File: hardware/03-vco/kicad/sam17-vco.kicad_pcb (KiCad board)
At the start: 4 copper layers, 114 x 124 mm, 140 parts, among them J1 Molex_KK-254_AE-6410-04A_1x04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, J2 IDC-Header_2x06_P2.54mm_Verti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, U1 QFN-32-1EP_4x4mm_P0.4mm_EP2.6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, U10 SOIC-14_3.9x8.7mm_P1.27mm, U11 SOT-89-3, U12 SOT-223-3_TabPin2, U13 VSSOP-8_3x3mm_P0.65mm, U14 SOT-23-5, U2 QFN-32-1EP_4x4mm_P0.4mm_EP2.6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, U3 QFN-32-1EP_4x4mm_P0.4mm_EP2.6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, U4 QFN-32-1EP_4x4mm_P0.4mm_EP2.6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, U5 TSSOP-16_4.4x5mm_P0.65mm, U6 TSSOP-16_4.4x5mm_P0.65mm, U7 TSSOP-16_4.4x5mm_P0.65mm, U8 SOIC-8_3.9x4.9mm_P1.27mm, U9 SOIC-14_3.9x8.7mm_P1.27mm

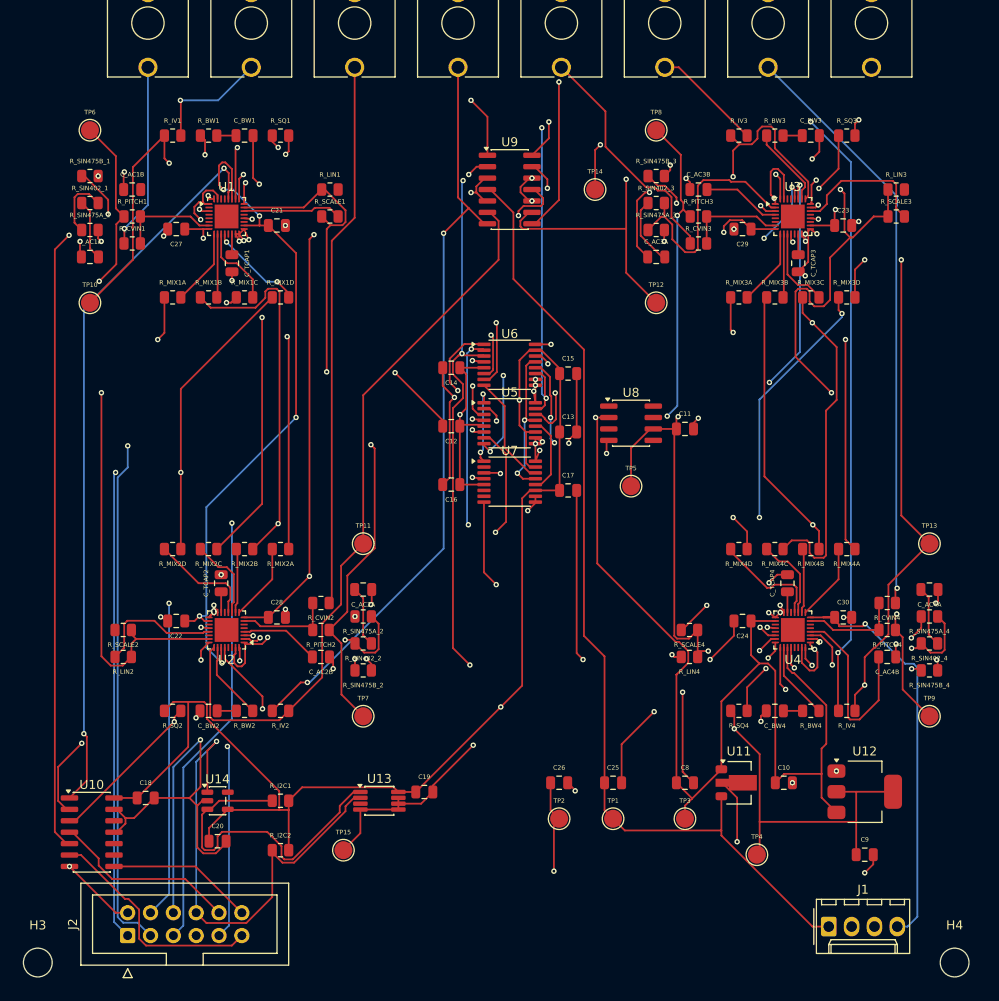
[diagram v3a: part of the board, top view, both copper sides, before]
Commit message: Modulo 3 VCO: los escapes explicitos se miden y se descartan (Tarea 6, ronda 5)
El controlador autorizo escribir escapes explicitos (pin -> via, cortos,
antes del ruteo, protegidos en el DSN) para el abanico del costado derecho
de los QFN, con la misma filosofia que las siete costuras de masa. Lo
implemente tal cual y lo medi en dos variantes. Sale peor, consistente:

  sin escapes de senal (cinco corridas):        4, 5, 8, 9, 10 abiertas
  + 20 escapes (pines 2,3,4,21,22), protegidos: 16
  + 8 escapes (solo 21 y 22), protegidos ronda 1: 12
  revertido a solo costuras de masa (comiteado): 11

Las dos variantes de escape quedan por debajo del PEOR sorteo del baseline,
asi que no es mala suerte.

La diferencia con las costuras de masa, que si funcionaron, es si el pin
tiene alternativa. El pin 20 del QFN y el 4 del TSSOP tienen un pasillo de
1 a 1.45 mm que da para una via y nada mas: reservarla es ganancia neta
porque le quitamos al router un sitio que no le servia para otra cosa. Los
pines 21 y 22 SI tienen alternativas -- arriba, abajo, en diagonal,
compartiendo carril -- y al reservarles una via les fijamos una sola salida
y ademas le quitamos a los otros veintisiete pines del mismo anillo el hueco
que necesitaban para su propio fanout. En el anillo de un QFN de 0.4 mm de
paso el cobre es un juego de suma cero, y el router reparte mejor que yo.

La leccion, que queda escrita en el script junto a los numeros: pre-colocar
funciona donde la geometria fuerza una unica solucion y estorba donde hay
varias.

DONDE QUEDA: DRC 0, In1 sin pistas y al 99.97% en una isla, costuras de masa
cerradas (0 pads sin bajada), frontera 3.00 mm, los 4 EP aislados, DAC->VCO
43.2 mm, desacoplos a 1.80 mm. Quedan 11 conexiones abiertas, diez de ellas
pines de QFN que no atraviesan su propio anillo de escape (1, 2, 21, 22, 23,
25, 26, 31: siempre los que van detras en la cola de su costado). Van en el
reporte con coordenada y motivo. El numero depende de la semilla del router
y no del dise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
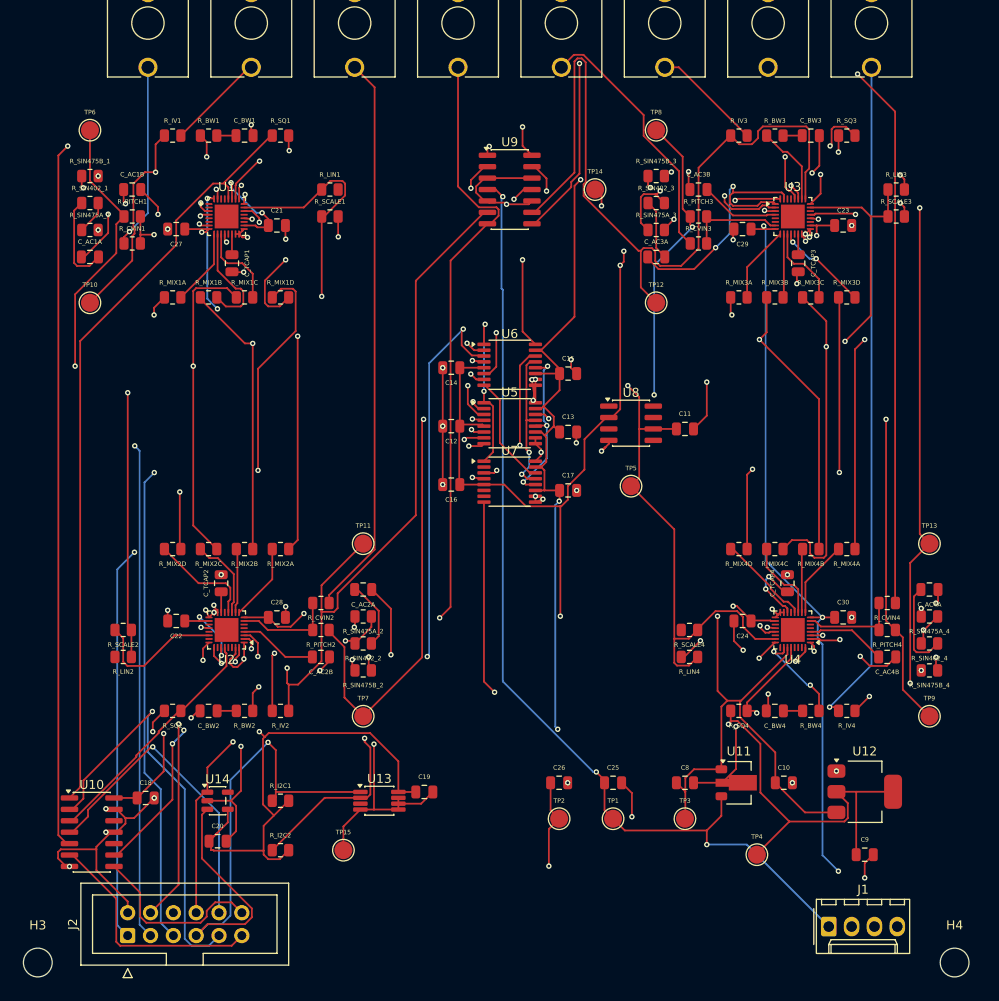
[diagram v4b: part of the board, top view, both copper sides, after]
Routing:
- net SQ_4: track 11.2 -> 92.1 mm, vias 2 -> 3
- net GNDA: track 170.1 -> 125.0 mm, vias 82 -> 76
- net VREF_2V5: track 292.8 -> 259.0 mm, vias 11 -> 6
- net GNDD: track 112.6 -> 79.9 mm, vias 4 -> 8
- net MIX_SAW: track 152.0 -> 120.8 mm, vias 4 -> 3
- net MIXO_3: track 61.6 -> 92.1 mm, vias 2 -> 0
- net I2C_SDA: track 36.8 -> 63.8 mm, vias 0 -> 1
- net MIX_TRI: track 116.0 -> 140.0 mm
- net N21_3: track 0.00 -> 19.9 mm, vias 0 -> 2
- net +5V_LOC: track 308.7 -> 293.2 mm, vias 10 -> 11
- net N22_2: track 0.00 -> 15.1 mm
- net TUNE_OUT_2: track 20.8 -> 35.1 mm, vias 0 -> 1
- net N21_2: track 14.3 -> 0.00 mm
- net N22_3: track 15.6 -> 1.69 mm, vias 0 -> 1
- net N22_4: track 13.0 -> 0.00 mm, vias 2 -> 0
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
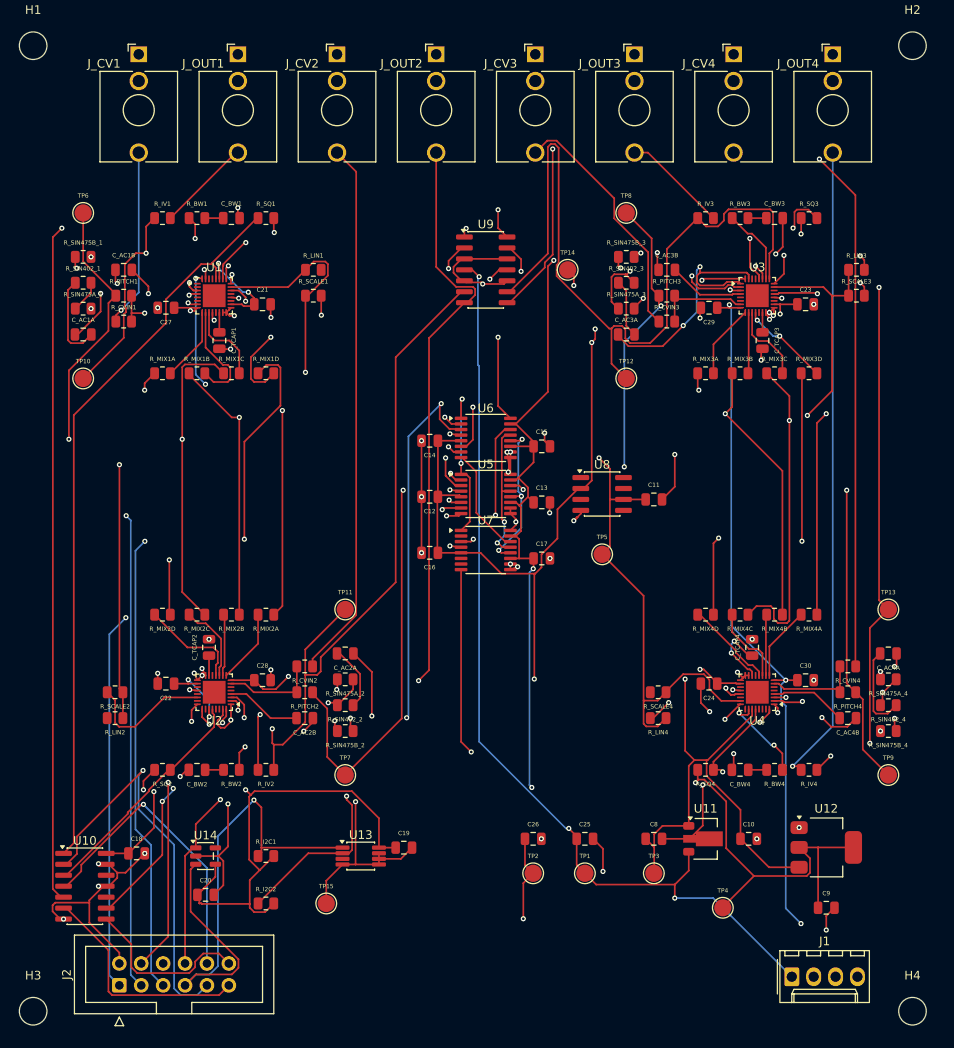
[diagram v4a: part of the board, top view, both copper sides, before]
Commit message: Modulo 3 VCO: reglas a la capacidad real del fab, y la placa CIERRA (Tarea 6)
0 conexiones abiertas y DRC 0. Con todos los demas gates en verde: In1 en
UNA sola isla al 100.00%, costuras de masa cerradas, frontera 3.00 mm, los
4 EP aislados, DAC->VCO 43.2 mm, desacoplos a 1.80 mm. El recorrido de la
tarea fue 165 -> 18 (2 capas) -> 8 -> 11 -> 0.

Las dos "paredes aritmeticas" que declare en la ronda 6 eran de MIS reglas,
no del fabricante. Via 0.6, margen 0.15 y pista 0.2 venian heredadas del
modulo 2 -- una placa de dos capas con componentes de paso ancho -- y nunca
les volvi a preguntar nada. Calcule bien y verifique mal: la formula
VIA_D/2 + CLEARANCE + ANCHO/2 = 0.55 > 0.40 era correcta, pero no mire la
hoja de capacidades del fabricante ni una sola vez antes de escribir
"taladro laser, proceso HDI, otra liga".

Verificado en jlcpcb.com/capabilities/pcb-capabilities el 2026-08-17,
proceso ESTANDAR de 4 capas en 1 oz, sin HDI y sin via-in-pad: pista y
aislamiento minimos 0.09/0.09 mm, taladro de via minimo 0.15, y sin recargo
un taladro de 0.20 si el diametro es >= 0.45 ("0.2mm or 0.25mm hole size
with via diameter less than 0.45mm, will cost more" -- por eso 0.45 y no el
0.40 sugerido: 0.45/0.20 es justo el punto sin recargo). Las reglas quedan
en pista 0.12, aislamiento 0.10, via 0.45/0.20: un 30% por encima del minimo
publicado. La aritmetica del escape pasa de 0.550 a 0.385 contra los 0.400
de paso del QFN, y queda como comprobacion ejecutable en _check_escape().

Con eso el ruteo cerro entero, pero aparecieron 108 infracciones de
hole_clearance: otro default de KiCad (0.25 mm) que tampoco habia elegido
nadie. El fabricante pide 0.20 de taladro de via a pista y el ruteo consigue
0.235 (anillo 0.125 + margen 0.11). Puesto el valor verificado, 0
infracciones -- no es relajar el checker, es que examinaba de una regla
inventada. KiCad tiene un solo campo de margen de taladro y el fabricante
pide 0.28 para PTH, asi que ese caso lo comprobe aparte sobre los 44
tala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
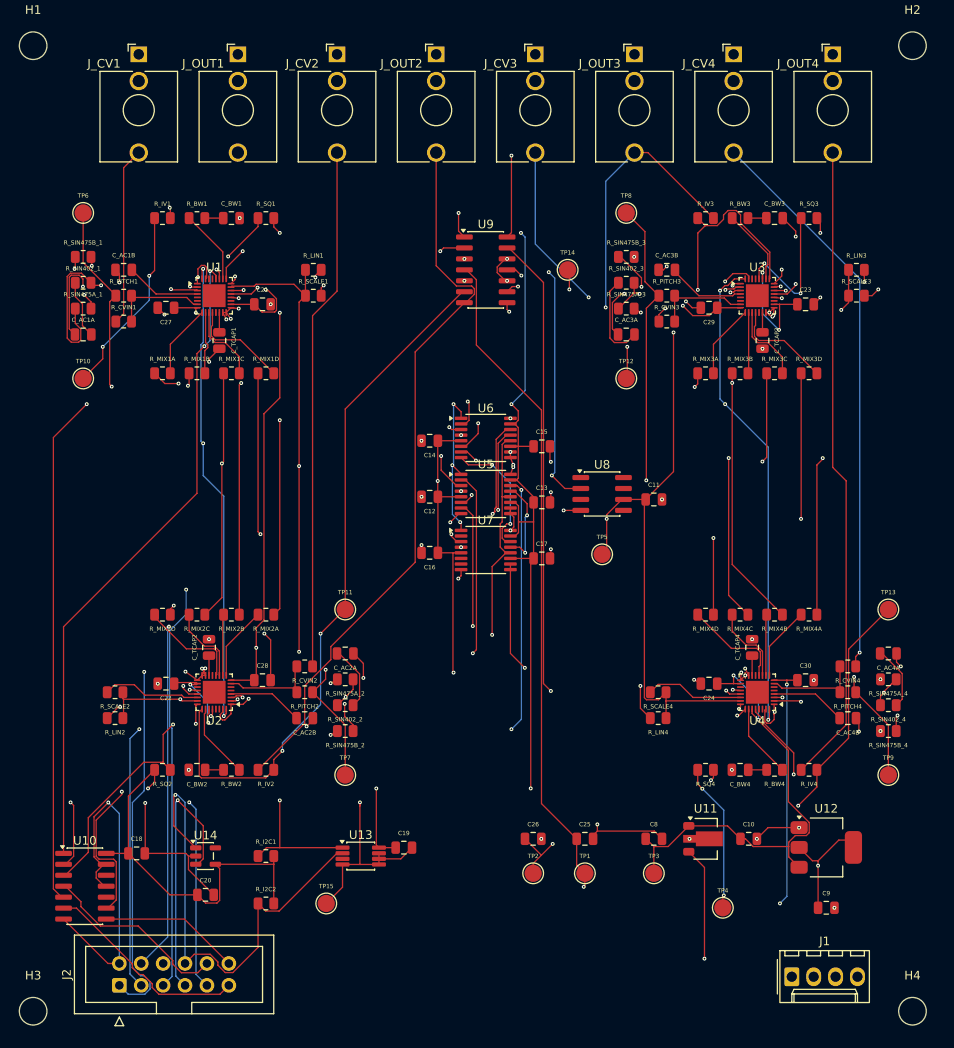
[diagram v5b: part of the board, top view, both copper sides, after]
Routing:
- net GNDA: track 125.0 -> 85.9 mm, vias 76 -> 82
- net MIXO_3: track 92.1 -> 55.9 mm, vias 0 -> 3
- net GNDD: track 79.9 -> 110.3 mm, vias 8 -> 4
- net N2_1: track 3.76 -> 28.9 mm, vias 0 -> 2
- net VREF_2V5: track 259.0 -> 234.9 mm, vias 6 -> 10
- net MIX_PULSE: track 145.5 -> 123.7 mm, vias 3 -> 4
- net PWM_CV: track 193.6 -> 176.2 mm
- net SQ_4: track 92.1 -> 106.8 mm
- net N22_3: track 1.69 -> 16.4 mm, vias 1 -> 2
- net +3V3_LOC: track 323.6 -> 309.5 mm, vias 9 -> 10
- net N21_2: track 0.00 -> 13.8 mm, vias 0 -> 2
- net TUNE_OUT_2: track 35.1 -> 21.8 mm, vias 1 -> 0
- net -12V: track 273.2 -> 260.4 mm, vias 7 -> 8
- net N21_1: track 0.00 -> 11.7 mm, vias 0 -> 2
- net CV_PITCH_4: track 85.7 -> 74.2 mm
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
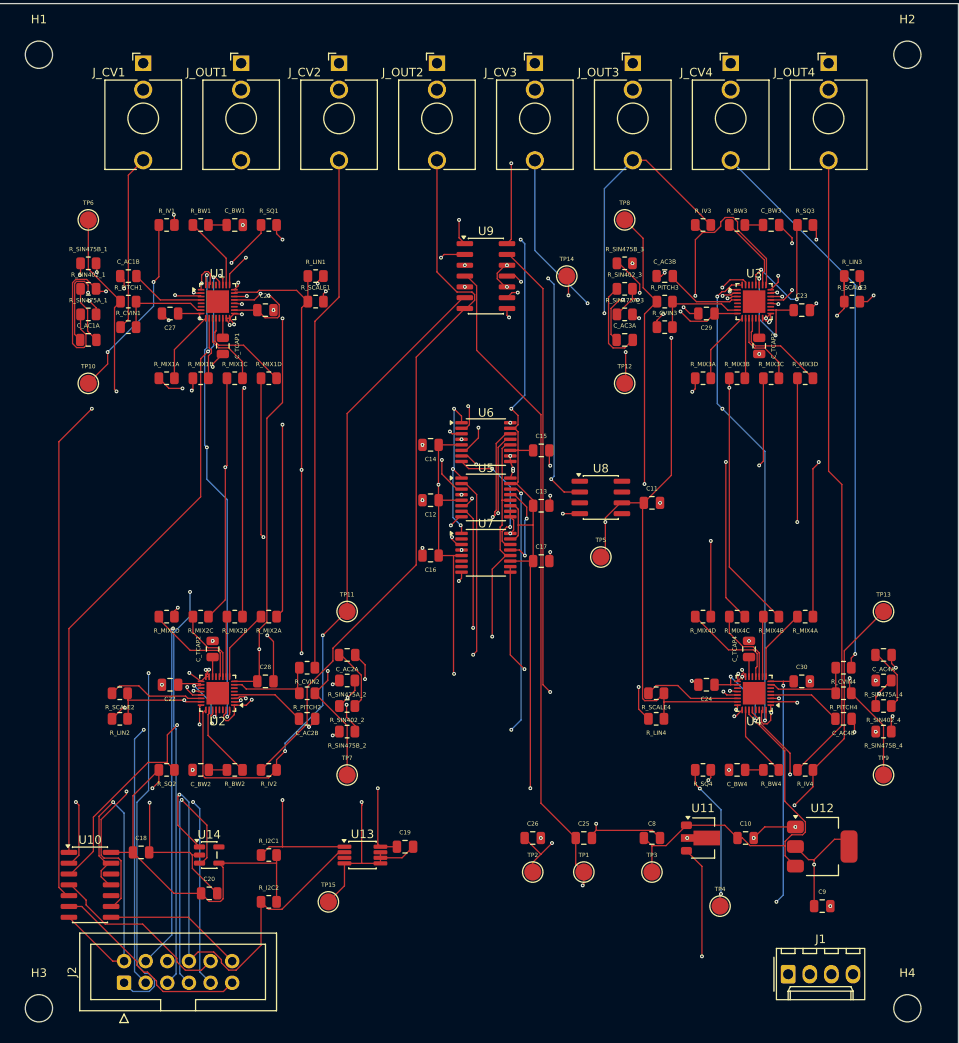
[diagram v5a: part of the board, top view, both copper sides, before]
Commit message: Modulo 3 VCO: vias fuera de los pads, serigrafia legible y U13 con los osciladores
La placa de la tanda anterior pasaba el gate porque el gate no miraba. Con
hole_to_hole y holes_co_located en la severidad que les corresponde, aquella
placa tiene 33 infracciones: 15 vias taladradas DENTRO del agujero de un jack
o de un conector (solapes de -0.81 mm, la broca pasando dos veces por el mismo
punto), 32 vias debajo de un pad SMD, y 3 parejas de vias por debajo del
minimo de taladro a taladro, una a 0.0000 mm.

El origen eran tres cosas y solo dos estaban a la vista. coser_masas() probaba
el CENTRO DEL PAD como primer sitio para la via. lejos() se salta el cobre de
la propia red -- correcto para un corto, equivocado para una broca, que no lee
el netlist. Y la tercera, que producia las ocho peores: en el manguito de un
jack el pad ESTA en el centro de la huella, asi que el rumbo del abanico salia
(0,0) y sus 110 candidatos degeneraban en un unico punto, el propio centro del
pad; con el yield del centro delante nadie lo noto en siete rondas.

Ahora el margen electrico y el mecanico son dos funciones con dos significados
-- lejos() y taladro_libre() --, la via va AL LADO del pad con su rabito (el
pasillo de 1 a 1.45 mm de la ronda 4 da para eso con via de 0.45), las dos
reglas de taladro son ERROR en el .kicad_pro, y revisar_taladros() lo vuelve a
medir sobre la placa terminada preguntandole a la FORMA real del pad y no a su
caja. Esa comprobacion se gano el sueldo: su primer falso positivo obligo a
medir bien, y al medir bien aparecio un defecto que nadie tenia visto, cuatro
vias de masa taladradas sobre la corona de los jacks.

La serigrafia iba a 0.5 mm de alto citando el minimo de PISTA del fabricante.
La misma hoja pide 1.0 mm de alto y 0.15 de trazo para el texto, y son dos
especificaciones distintas. Eran 112 avisos de text_height y una placa que
violaba su propio minimo declarado. Se arregla como lo hace la industria en
SMD: se ocultan las referencias de los pasivos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
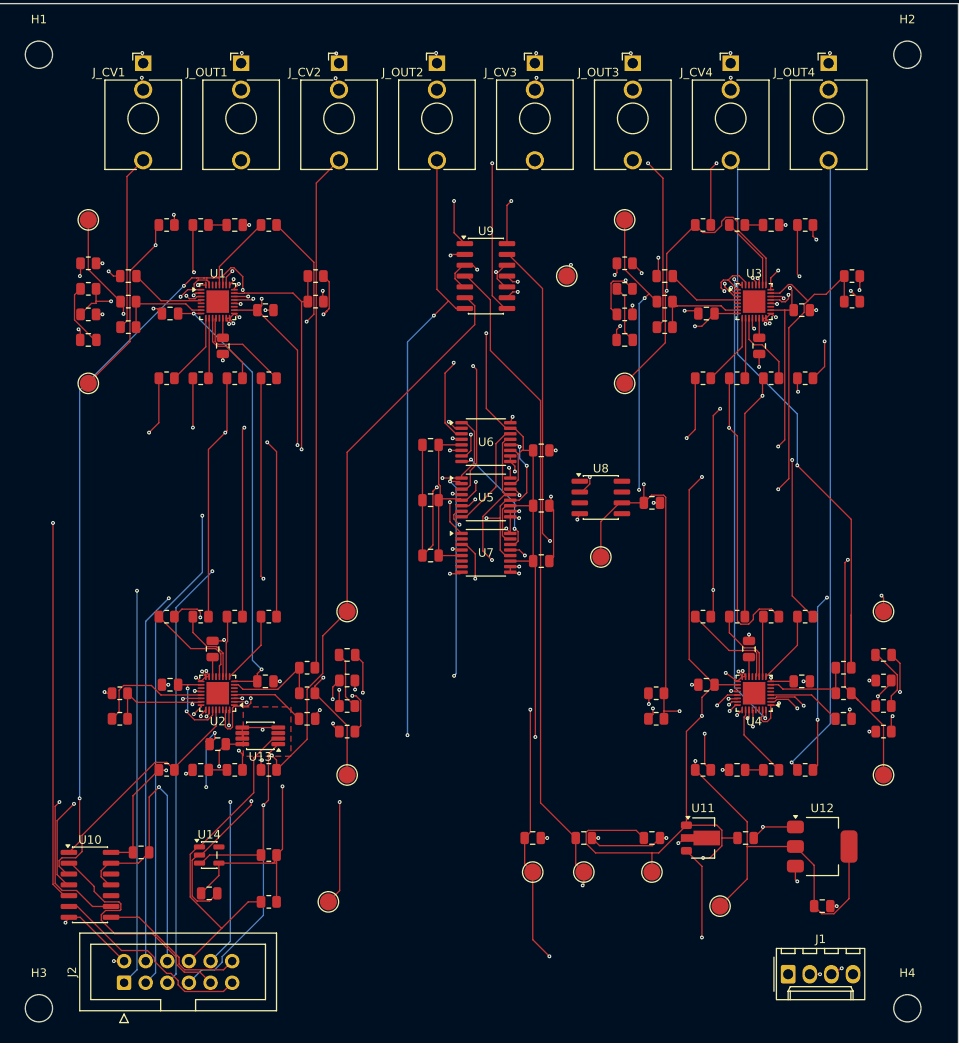
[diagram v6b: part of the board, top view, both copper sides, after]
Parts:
- moved C19 25.1 mm to (27.0, 87.0), turned to 180 degrees
- moved U13 18.4 mm to (32.0, 86.0), turned to 180 degrees
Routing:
- net GNDA: track 85.9 -> 136.9 mm, vias 82 -> 79
- net PWM_CV: track 176.2 -> 206.9 mm, vias 7 -> 5
- net VREF_2V5: track 234.9 -> 262.4 mm, vias 10 -> 8
- net TUNE_OUT_2: track 21.8 -> 49.1 mm, vias 0 -> 2
- net +5V_LOC: track 295.5 -> 318.0 mm, vias 12 -> 15
- net I2C_SCL: track 56.7 -> 39.9 mm, vias 1 -> 0
- net TUNE_OUT_1: track 44.3 -> 28.6 mm, vias 2 -> 0
- net SQ_3: track 164.0 -> 151.8 mm
- net N2_1: track 28.9 -> 16.8 mm
- net I2C_SDA: track 58.8 -> 46.8 mm, vias 2 -> 1
- net GNDD: track 110.3 -> 120.3 mm, vias 4 -> 8
- net VOICE_OUT_3: track 44.2 -> 53.2 mm
- net MIXO_4: track 118.3 -> 111.1 mm, vias 3 -> 5
- net TRI_1: track 27.9 -> 20.7 mm
- net VOICE_OUT_2: track 85.0 -> 91.9 mm, vias 0 -> 3
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- added copper zone on F.Cu, net (none)
